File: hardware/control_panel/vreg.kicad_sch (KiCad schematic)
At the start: 22 parts, among them U5 AP64352

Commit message: hw layout
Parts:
- removed C13: 22u, Capacitor_SMD:C_0805_2012Metric, symbol Device:C
- added C2, C6: 22u, Capacitor_SMD:C_0805_2012Metric, symbol Device:C
- C17, C3: footprint Capacitor_THT:CP_Radial_D10.0mm_P5.00mm -> Capacitor_THT:CP_Radial_D8.0mm_P3.50mm
- L2: footprint Inductor_THT:L_Radial_D7.5mm_P5.00mm_Fastron_07P -> Inductor_THT:L_Radial_D7.5mm_P3.50mm_Fastron_07P
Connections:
- net +5V: now also C2.1, C6.1
- net GND: now also C2.2, C6.2
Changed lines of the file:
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@@
       (effects (font (size 1.27 1.27)) (justify left))
     )
-    (property "Footprint" "Capacitor_THT:CP_Radial_D10.0mm_P5.00mm" (at 26.3652 85.09 0)
+    (property "Footprint" "Capacitor_THT:CP_Radial_D8.0mm_P3.50mm" (at 26.3652 85.09 0)
       (effects (font (size 1.27 1.27)) hide)
     )
@@
     )
   )
+  (symbol (lib_id "power:+5V") (at 220.98 72.39 0) (unit 1)
+    (in_bom yes) (on_board yes) (dnp no) (fields_autoplaced)
+    (property "Reference" "#PWR023" (at 220.98 76.2 0)
+      (effects (font (size 1.27 1.27)) hide)
+    )
+    (property "Value" "~" (at 220.98 68.8142 0)
+      (effects (font (size 1.27 1.27)))
+    )
+    (property "Footprint" "" (at 220.98 72.39 0)
+      (effects (font (size 1.27 1.27)) hide)
+    )
+    (property "Datasheet" "" (at 220.98 72.39 0)
+      (effects (font (size 1.27 1.27)) hide)
+    )
+    (pin "1")
+    (instances
+      (project "control_panel"
+        (path "/e63e39d7-6ac0-4ffd-8aa3-1841a4541b55/a07b7207-b2ba-4964-b1bd-fe9eb7be7391"
+          (reference "#PWR023") (unit 1)
+        )
+      )
+    )
+  )
   (symbol (lib_id "power:GND") (at 120.65 121.92 0) (unit 1)
     (in_bom yes) (on_board yes) (dnp no) (fields_autoplaced)
@@
     )
   )
+  (symbol (lib_id "Device:C") (at 246.38 76.2 0) (unit 1)
+    (in_bom yes) (on_board yes) (dnp no) (fields_autoplaced)
+    (property "Reference" "C6" (at 249.301 75.3653 0)
+      (effects (font (size 1.27 1.27)) (justify left))
+    )
+    (property "Value" "22u" (at 249.301 77.9022 0)
+      (effects (font (size 1.27 1.27)) (justify left))
+    )
+    (property "Footprint" "Capacitor_SMD:C_0805_2012Metric" (at 247.3452 80.01 0)
+      (effects (font (size 1.27 1.27)) hide)
+    )
+    (property "Datasheet" "~" (at 246.38 76.2 0)
+      (effects (font (size 1.27 1.27)) hide)
+    )
+    (pin "1")
+    (pin "2")
+    (instances
+      (project "control_panel"
+        (path "/e63e39d7-6ac0-4ffd-8aa3-1841a4541b55/a07b7207-b2ba-4964-b1bd-fe9eb7be7391"
+          (reference "C6") (unit 1)
+        )
+      )
+    )
+  )
   (symbol (lib_id "power:+24V") (at 38.1 72.39 0) (unit 1)
     (in_bom yes) (on_board yes) (dnp no) (fields_autoplaced)
@@
         (path "/e63e39d7-6ac0-4ffd-8aa3-1841a4541b55/a07b7207-b2ba-4964-b1bd-fe9eb7be7391"
           (reference "#PWR0151") (unit 1)
+        )
+      )
+    )
+  )
+  (symbol (lib_id "power:GND") (at 220.98 80.01 0) (unit 1)
+    (in_bom yes) (on_board yes) (dnp no) (fields_autoplaced)
+    (property "Reference" "#PWR024" (at 220.98 86.36 0)
+      (effects (font (size 1.27 1.27)) hide)
+    )
+    (property "Value" "~" (at 220.98 84.4534 0)
+      (effects (font (size 1.27 1.27)))
+    )
+    (property "Footprint" "" (at 220.98 80.01 0)
+      (effects (font (size 1.27 1.27)) hide)
+    )
+    (property "Datasheet" "" (at 220.98 80.01 0)
+      (effects (font (size 1.27 1.27)) hide)
+    )
+    (pin "1")
+    (instances
+      (project "control_panel"
+        (path "/e63e39d7-6ac0-4ffd-8aa3-1841a4541b55/a07b7207-b2ba-4964-b1bd-fe9eb7be7391"
+          (reference "#PWR024") (unit 1)
         )
       )
@@
     )
   )
-  (symbol (lib_id "power:+5V") (at 219.71 72.39 0) (unit 1)
-    (in_bom yes) (on_board yes) (dnp no) (fields_autoplaced)
-    (property "Reference" "#PWR0148" (at 219.71 76.2 0)
-      (effects (font (size 1.27 1.27)) hide)
-    )
-    (property "Value" "~" (at 219.71 68.8142 0)
-      (effects (font (size 1.27 1.27)))
-    )
-    (property "Footprint" "" (at 219.71 72.39 0)
-      (effects (font (size 1.27 1.27)) hide)
-    )
-    (property "Datasheet" "" (at 219.71 72.39 0)
-      (effects (font (size 1.27 1.27)) hide)
-    )
-    (pin "1")
-    (instances
-      (project "control_panel"
-        (path "/e63e39d7-6ac0-4ffd-8aa3-1841a4541b55/a07b7207-b2ba-4964-b1bd-fe9eb7be7391"
-          (reference "#PWR0148") (unit 1)
-        )
-      )
-    )
-  )
   (symbol (lib_id "Device:C") (at 148.59 128.27 0) (unit 1)
     (in_bom yes) (on_board yes) (dnp no) (fields_autoplaced)
@@
       (effects (font (size 1.27 1.27)) (justify left))
     )
-    (property "Footprint" "Capacitor_THT:CP_Radial_D10.0mm_P5.00mm" (at 84.7852 80.01 0)
+    (property "Footprint" "Capacitor_THT:CP_Radial_D8.0mm_P3.50mm" (at 84.7852 80.01 0)
       (effects (font (size 1.27 1.27)) hide)
     )
@@
     )
   )
+  (symbol (lib_id "power:GND") (at 246.38 80.01 0) (unit 1)
+    (in_bom yes) (on_board yes) (dnp no) (fields_autoplaced)
+    (property "Reference" "#PWR046" (at 246.38 86.36 0)
+      (effects (font (size 1.27 1.27)) hide)
+    )
+    (property "Value" "~" (at 246.38 84.4534 0)
+      (effects (font (size 1.27 1.27)))
+    )
+    (property "Footprint" "" (at 246.38 80.01 0)
+      (effects (font (size 1.27 1.27)) hide)
+    )
+    (property "Datasheet" "" (at 246.38 80.01 0)
+      (effects (font (size 1.27 1.27)) hide)
+    )
+    (pin "1")
+    (instances
+      (project "control_panel"
+        (path "/e63e39d7-6ac0-4ffd-8aa3-1841a4541b55/a07b7207-b2ba-4964-b1bd-fe9eb7be7391"
+          (reference "#PWR046") (unit 1)
+        )
+      )
+    )
+  )
   (symbol (lib_id "power:+24V") (at 95.25 102.87 0) (unit 1)
     (in_bom yes) (on_board yes) (dnp no) (fields_autoplaced)
@@
       (effects (font (size 1.27 1.27)))
     )
-    (property "Footprint" "Inductor_THT:L_Radial_D7.5mm_P5.00mm_Fastron_07P" (at 31.75 74.93 0)
+    (property "Footprint" "Inductor_THT:L_Radial_D7.5mm_P3.50mm_Fastron_07P" (at 31.75 74.93 0)
       (effects (font (size 1.27 1.27)) hide)
     )
@@
     )
   )
+  (symbol (lib_id "power:+5V") (at 246.38 72.39 0) (unit 1)
+    (in_bom yes) (on_board yes) (dnp no) (fields_autoplaced)
+    (property "Reference" "#PWR025" (at 246.38 76.2 0)
+      (effects (font (size 1.27 1.27)) hide)
+    )
+    (property "Value" "~" (at 246.38 68.8142 0)
+      (effects (font (size 1.27 1.27)))
+    )
+    (property "Footprint" "" (at 246.38 72.39 0)
+      (effects (font (size 1.27 1.27)) hide)
+    )
+    (property "Datasheet" "" (at 246.38 72.39 0)
+      (effects (font (size 1.27 1.27)) hide)
+    )
+    (pin "1")
+    (instances
+      (project "control_panel"
+        (path "/e63e39d7-6ac0-4ffd-8aa3-1841a4541b55/a07b7207-b2ba-4964-b1bd-fe9eb7be7391"
+          (reference "#PWR025") (unit 1)
+        )
+      )
+    )
+  )
   (symbol (lib_id "Device:R") (at 120.65 105.41 0) (unit 1)
     (in_bom yes) (on_board yes) (dnp no) (fields_autoplaced)
@@
         (path "/e63e39d7-6ac0-4ffd-8aa3-1841a4541b55/a07b7207-b2ba-4964-b1bd-fe9eb7be7391"
           (reference "#PWR0152") (unit 1)
-        )
-      )
-    )
-  )
-  (symbol (lib_id "power:GND") (at 219.71 80.01 0) (unit 1)
-    (in_bom yes) (on_board yes) (dnp no) (fields_autoplaced)
-    (property "Reference" "#PWR0147" (at 219.71 86.36 0)
-      (effects (font (size 1.27 1.27)) hide)
-    )
-    (property "Value" "~" (at 219.71 84.4534 0)
-      (effects (font (size 1.27 1.27)))
-    )
-    (property "Footprint" "" (at 219.71 80.01 0)
-      (effects (font (size 1.27 1.27)) hide)
-    )
-    (property "Datasheet" "" (at 219.71 80.01 0)
-      (effects (font (size 1.27 1.27)) hide)
-    )
-    (pin "1")
-    (instances
-      (project "control_panel"
-        (path "/e63e39d7-6ac0-4ffd-8aa3-1841a4541b55/a07b7207-b2ba-4964-b1bd-fe9eb7be7391"
-          (reference "#PWR0147") (unit 1)
         )
       )
@@
     )
   )
+  (symbol (lib_id "Device:C") (at 220.98 76.2 0) (unit 1)
+    (in_bom yes) (on_board yes) (dnp no) (fields_autoplaced)
+    (property "Reference" "C2" (at 223.901 75.3653 0)
+      (effects (font (size 1.27 1.27)) (justify left))
+    )
+    (property "Value" "22u" (at 223.901 77.9022 0)
+      (effects (font (size 1.27 1.27)) (justify left))
+    )
+    (property "Footprint" "Capacitor_SMD:C_0805_2012Metric" (at 221.9452 80.01 0)
+      (effects (font (size 1.27 1.27)) hide)
+    )
+    (property "Datasheet" "~" (at 220.98 76.2 0)
+      (effects (font (size 1.27 1.27)) hide)
+    )
+    (pin "1")
+    (pin "2")
+    (instances
+      (project "control_panel"
+        (path "/e63e39d7-6ac0-4ffd-8aa3-1841a4541b55/a07b7207-b2ba-4964-b1bd-fe9eb7be7391"
+          (reference "C2") (unit 1)
+        )
+      )
+    )
+  )
   (symbol (lib_id "power:GND") (at 25.4 85.09 0) (unit 1)
     (in_bom yes) (on_board yes) (dnp no) (fields_autoplaced)
@@
         )
       )
-    )
-  )
-  (symbol (lib_id "Device:C") (at 219.71 76.2 0) (unit 1)
-    (in_bom yes) (on_board yes) (dnp no) (fields_autoplaced)
-    (property "Reference" "C13" (at 222.631 75.3653 0)
-      (effects (font (size 1.27 1.27)) (justify left))
-    )
-    (property "Value" "22u" (at 222.631 77.9022 0)
-      (effects (font (size 1.27 1.27)) (justify left))
-    )
-    (property "Footprint" "Capacitor_SMD:C_0805_2012Metric" (at 220.6752 80.01 0)
-      (effects (font (size 1.27 1.27)) hide)
-    )
-    (property "Datasheet" "~" (at 219.71 76.2 0)
-      (effects (font (size 1.27 1.27)) hide)
-    )
-    (pin "1")
-    (pin "2")
-    (instances
-      (project "control_panel"
-        (path "/e63e39d7-6ac0-4ffd-8aa3-1841a4541b55/a07b7207-b2ba-4964-b1bd-fe9eb7be7391"
-          (reference "C13") (unit 1)
-        )
-      )

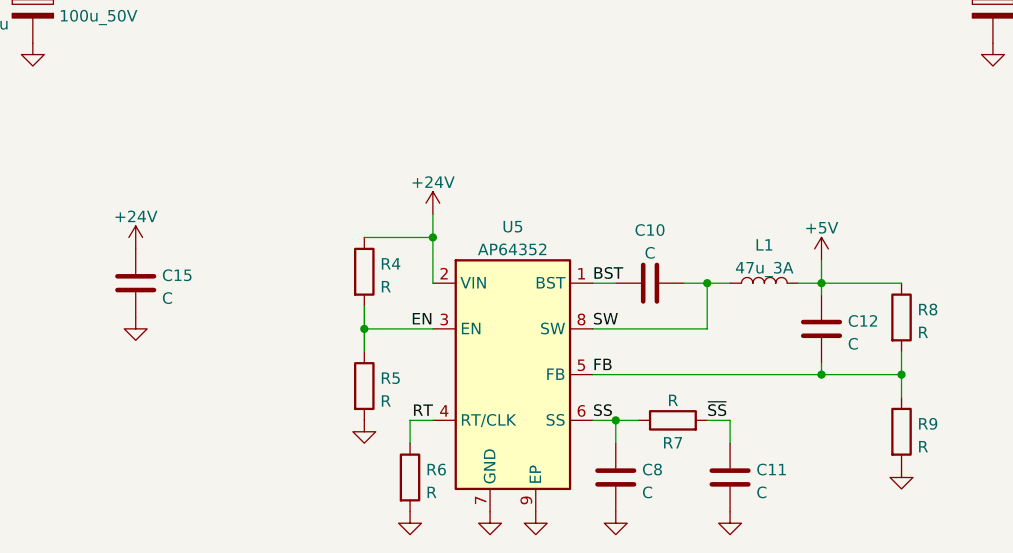
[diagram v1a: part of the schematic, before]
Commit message: led balance and corridor ready
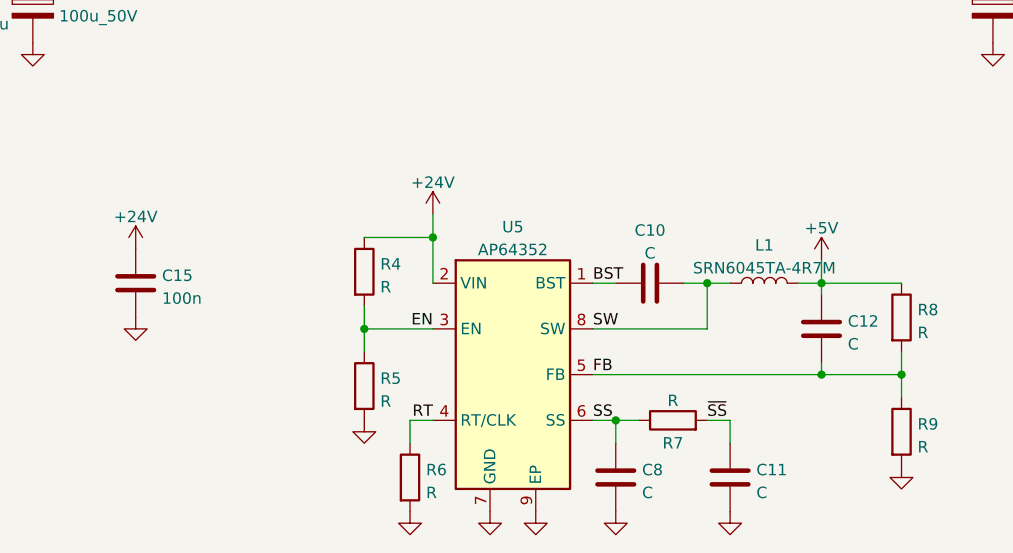
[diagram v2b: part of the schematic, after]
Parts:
- C15: value C -> 100n
- L1: value 47u_3A -> SRN6045TA-4R7M
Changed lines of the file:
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@@
       (effects (font (size 1.27 1.27)))
     )
-    (property "Value" "47u_3A" (at 165.1 105.0091 90)
+    (property "Value" " SRN6045TA-4R7M" (at 165.1 105.0091 90)
       (effects (font (size 1.27 1.27)))
     )
@@
       (effects (font (size 1.27 1.27)) (justify right))
     )
-    (property "Value" "C" (at 98.171 108.3822 0)
+    (property "Value" "100n" (at 98.171 108.3822 0)
       (effects (font (size 1.27 1.27)) (justify right))
     )
